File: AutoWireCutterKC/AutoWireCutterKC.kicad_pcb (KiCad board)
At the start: 2 copper layers, 17 parts, among them J1 LCD I/O, J2 ISP, J3 LCD Serial, J5 LCD Power, J6 Servo, J8 Barrel_Jack, J9 Stepper, U1 ATMEGA328P-AU, U2 MCP1700_SOT23, U3 LT1129-5.0_SOT223

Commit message: PCB Populated
Traces needed
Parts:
- removed J3: LCD Serial, Pin_Headers:Pin_Header_Angled_1x02_Pitch2.54mm
- removed J5: LCD Power, Pin_Headers:Pin_Header_Angled_1x02_Pitch2.54mm
- removed J6: Servo, Pin_Headers:Pin_Header_Angled_1x03_Pitch2.54mm
- added +5v: LCD Power, Pin_Headers:Pin_Header_Angled_1x02_Pitch2.54mm, F.Cu at (159.5, 117.3)
- added RX: LCD Serial, Pin_Headers:Pin_Header_Angled_1x02_Pitch2.54mm, F.Cu at (167.1, 117.3)
- added Servo: Servo, Pin_Headers:Pin_Header_Angled_1x03_Pitch2.54mm, F.Cu at (148.3, 117.3)
- moved C3 54.8 mm to (166.4, 81.3), turned to 180 degrees
- moved U3 51.5 mm to (170.2, 100.3), turned to 270 degrees
- moved C5 49.4 mm to (170.2, 94.0), turned to 180 degrees
- moved C1 41.5 mm to (161.3, 90.2)
- moved C2 39.4 mm to (158.8, 85.1)
- moved U2 29.3 mm to (166.4, 85.1), turned to 90 degrees
- moved C4 27.1 mm to (156.2, 90.2)
- moved C6 23.2 mm to (168.9, 90.2)
- moved J1 22.7 mm to (160.0, 105.4)
- moved J2 18.0 mm to (168.9, 108.0)
- moved A1 16.4 mm to (137.7, 96.0)
- moved U1 8.77 mm to (158.0, 97.0)
- moved J8 7.64 mm to (147.3, 91.4), turned to 180 degrees
- moved J9 5.61 mm to (154.9, 105.4)
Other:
- board outline added: 39.1 x 41.7 mm
- board text added: "Auto Wire Cutter"
- board text added: "BRW"

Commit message: Moving around footprints
Changing spacing and connectors
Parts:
- Servo: footprint Pin_Headers:Pin_Header_Angled_1x03_Pitch2.54mm -> Connectors_JST:JST_PH_S3B-PH-SM4-TB_03x2.00mm_Angled
- moved J2 18.3 mm to (165.6, 89.9)
- moved U3 17.5 mm to (166.1, 83.3)
- moved U2 16.2 mm to (150.4, 87.9)
- moved C3 12.3 mm to (156.0, 87.9)
- moved C6 11.2 mm to (160.5, 82.8), turned to 90 degrees
- moved C5 10.7 mm to (160.5, 89.4), turned to 270 degrees
- moved C1 10.5 mm to (150.9, 91.4)
- moved J1 7.73 mm to (165.6, 100.1)
- moved C2 6.02 mm to (153.4, 82.3)
- moved J8 4.06 mm to (143.3, 91.4)
- moved J9 0.57 mm to (155.4, 105.7)
- moved C4 0.36 mm to (156.0, 90.4)

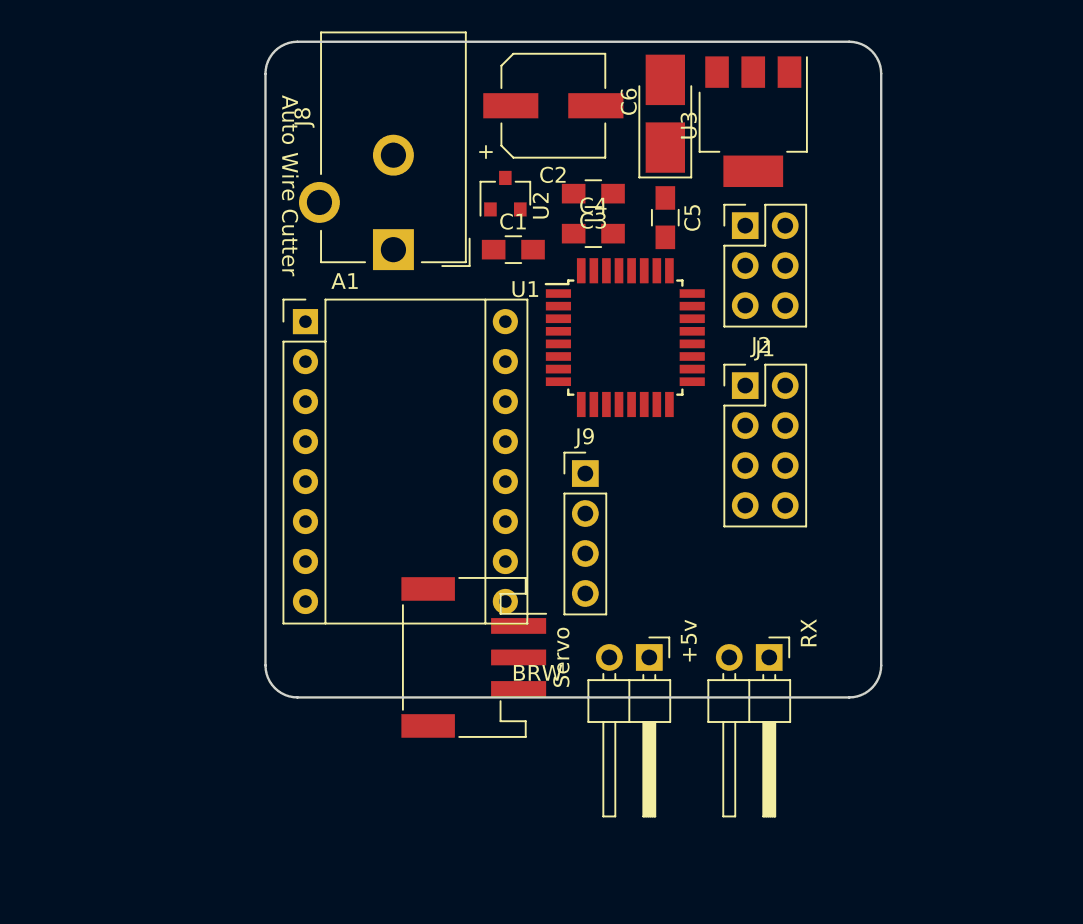
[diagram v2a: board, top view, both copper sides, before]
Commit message: PCB Redesign
Started on traces
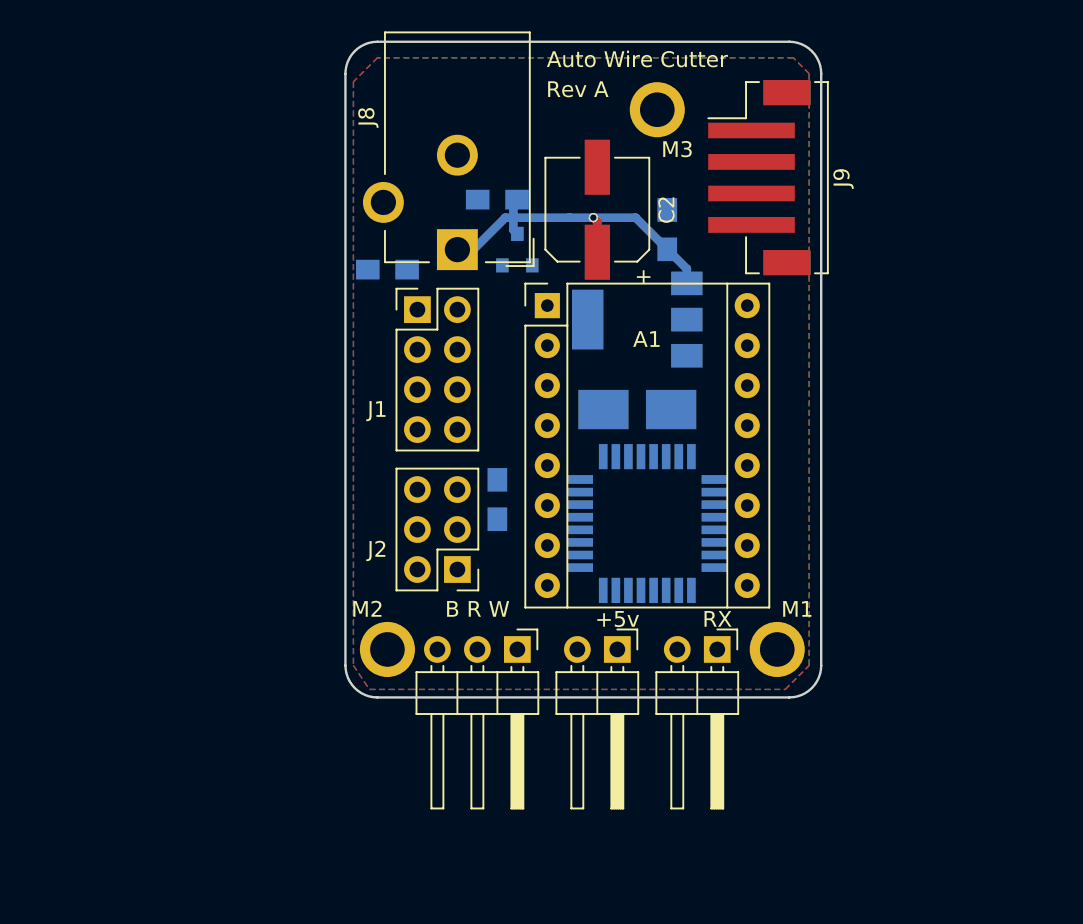
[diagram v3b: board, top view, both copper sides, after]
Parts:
- added M1: MountingHole_2.2mm_M2_ISO7380_Pad, Mounting_Holes:MountingHole_2.2mm_M2_ISO7380_Pad, F.Cu at (167.6, 116.8)
- added M2: MountingHole_2.2mm_M2_ISO7380_Pad, Mounting_Holes:MountingHole_2.2mm_M2_ISO7380_Pad, F.Cu at (142.9, 116.8)
- added M3: MountingHole_2.2mm_M2_ISO7380_Pad, Mounting_Holes:MountingHole_2.2mm_M2_ISO7380_Pad, F.Cu at (160.0, 82.5)
- B R W: renamed from Servo; footprint Connectors_JST:JST_PH_S3B-PH-SM4-TB_03x2.00mm_Angled -> Pin_Headers:Pin_Header_Angled_1x03_Pitch2.54mm
- C1, C3, C4, C5, C6, U1, U2, U3: moved to B.Cu
- J9: footprint Pin_Headers:Pin_Header_Straight_1x04_Pitch2.54mm -> Connectors_JST:JST_PH_B4B-PH-SM4-TB_04x2.00mm_Straight
- moved J2 28.5 mm to (147.3, 111.8), turned to 180 degrees
- moved J9 22.1 mm to (167.1, 86.9), turned to 270 degrees
- moved J1 21.4 mm to (144.8, 95.2)
- moved C6 18.9 mm to (158.8, 101.6), turned to 180 degrees
- moved C1 15.9 mm to (149.9, 107.3), turned to 90 degrees
- moved A1 15.4 mm to (153.0, 95.0)
- moved U3 14.6 mm to (158.8, 95.9), turned to 180 degrees
- moved C4 13.3 mm to (142.9, 92.7), turned to 180 degrees
- moved U1 11.9 mm to (159.4, 108.8), turned to 90 degrees
- moved C2 7.17 mm to (156.2, 88.9), turned to 90 degrees
- moved C3 6.11 mm to (149.9, 88.3)
- moved J8 4.06 mm to (147.3, 91.4)
- moved U2 3.64 mm to (151.1, 91.4)
- moved RX 3.34 mm to (163.8, 116.8)
- moved B R W 2.84 mm to (151.1, 116.8)
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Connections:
- J2 pad 2: +3V3 -> +5VL
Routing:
- net +12V: track 0.00 -> 22.4 mm, vias 0 -> 1
- added copper zone on F.Cu, net +5VL
- added copper zone on B.Cu, net GND
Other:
- board size 39.1 x 41.7 mm -> 30.2 x 41.7 mm
- net class 12v added: clearance 0.5, trace_width 0.55, via_dia 0.6, via_drill 0.4
- board text added: "Rev A"
- board text removed: "BRW"

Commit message: Rewiring - Layout changed again...
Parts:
- C1: moved to F.Cu
- J9: moved to B.Cu
- moved B R W 18.9 mm to (167.6, 107.7), turned to 0 degrees
- moved U1 16.6 mm to (142.7, 109.2), turned to 0 degrees
- moved C1 14.3 mm to (136.1, 111.3), turned to 270 degrees
- moved +5v 12.7 mm to (144.8, 116.8)
- moved RX 11.9 mm to (151.9, 116.8)
- moved C2 11.8 mm to (167.1, 84.3), turned to 270 degrees
- moved A1 11.8 mm to (162.1, 102.6), turned to 180 degrees
- moved M3 11.2 mm to (148.8, 81.3)
- moved J2 10.2 mm to (157.5, 110.7), turned to 0 degrees
- moved J9 9.16 mm to (167.6, 96.0), turned to 90 degrees
- moved J1 8.53 mm to (139.7, 102.1), turned to 180 degrees
- moved C5 7.10 mm to (155.4, 95.0), turned to 180 degrees
- moved U2 6.19 mm to (145.3, 93.5)
- moved U3 5.66 mm to (154.9, 100.1)
- moved J8 5.59 mm to (141.7, 91.4)
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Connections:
- J9 pad 1: Net-(A1-Pad4) -> Net-(A1-Pad3)
- J9 pad 2: Net-(A1-Pad3) -> Net-(A1-Pad4)
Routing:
- net Net-(J1-Pad4): track 0.00 -> 37.0 mm, vias 0 -> 2
- net Net-(A1-Pad9): track 0.00 -> 35.2 mm, vias 0 -> 1
- net Net-(J6-Pad1): track 0.00 -> 33.5 mm, vias 0 -> 1
- net Net-(J1-Pad6): track 0.00 -> 33.5 mm
- net Net-(J1-Pad5): track 0.00 -> 26.9 mm, vias 0 -> 1
- net +12V: track 22.4 -> 0.00 mm, vias 1 -> 0
- net Net-(J1-Pad7): track 0.00 -> 20.9 mm, vias 0 -> 1
- net Net-(J2-Pad5): track 0.00 -> 18.3 mm, vias 0 -> 1
- net Net-(J1-Pad8): track 0.00 -> 13.8 mm
- net Net-(J3-Pad1): track 0.00 -> 12.4 mm
- net Net-(J3-Pad2): track 0.00 -> 11.1 mm
- net Net-(J1-Pad2): track 0.00 -> 9.52 mm
- net Net-(J1-Pad3): track 0.00 -> 8.05 mm
- net Net-(J1-Pad1): track 0.00 -> 4.41 mm
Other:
- board size 30.2 x 41.7 mm -> 35.8 x 41.7 mm
- net class 12v: trace_width 0.55 -> 0.75; via_dia 0.6 -> 1; via_drill 0.4 -> 0.8
- net class MotorLeads added: clearance 0.25, trace_width 0.4, via_dia 0.6, via_drill 0.4

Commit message: Update bad file
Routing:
- net Net-(A1-Pad15): track 0.00 -> 25.2 mm, vias 0 -> 2
- net Net-(A1-Pad16): track 0.00 -> 20.6 mm, vias 0 -> 2
- net GND: track 0.00 -> 5.22 mm, vias 0 -> 2
- net +5VL: track 0.00 -> 3.83 mm, vias 0 -> 2
- net Net-(A1-Pad9): track 35.2 -> 38.9 mm, vias 1 -> 3
- net Net-(J1-Pad6): track 33.5 -> 33.3 mm, vias 0 -> 1

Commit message: Schematic almost done
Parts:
- M1, M2, M3: value MountingHole_2.2mm_M2_ISO7380_Pad -> Conn_01x01_Male
- moved M3 3.14 mm to (151.9, 80.5)
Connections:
- M1 pad 1: (no net) -> GND
- M2 pad 1: (no net) -> GND
- M3 pad 1: (no net) -> GND
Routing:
- net +12V: track 0.00 -> 58.1 mm, vias 0 -> 1
- net +5V: track 0.00 -> 14.2 mm
- net GND: track 5.22 -> 15.3 mm, vias 2 -> 3
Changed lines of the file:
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@@
 (kicad_pcb (version 4) (host pcbnew 4.0.7)
   (general
-    (links 59)
-    (no_connects 21)
-    (area 122.501333 76.714999 182.298667 127.915001)
+    (links 62)
+    (no_connects 10)
+    (area 134.544999 78.156999 170.509001 119.963001)
     (thickness 1.6)
     (drawings 12)
-    (tracks 131)
+    (tracks 164)
     (zones 0)
     (modules 20)
@@
   (page A4)
   (layers
-    (0 F.Cu signal hide)
+    (0 F.Cu signal)
     (31 B.Cu signal)
     (32 B.Adhes user)
@@
   )
   (module Mounting_Holes:MountingHole_2.2mm_M2_ISO7380_Pad (layer F.Cu)
-    (at 148.844 81.28)
+    (at 151.892 80.518)
     (descr "Mounting Hole 2.2mm, M2, ISO7380")
     (tags "mounting hole 2.2mm m2 iso7380")
     (attr virtual)
-    (fp_text reference M3 (at 1.27 2.54) (layer F.SilkS)
-      (effects (font (size 1 1) (thickness 0.15)))
-    )
-    (fp_text value MountingHole_2.2mm_M2_ISO7380_Pad (at 0 2.75) (layer F.Fab)
+    (fp_text reference M3 (at -3.302 -0.762) (layer F.SilkS)
+      (effects (font (size 1 1) (thickness 0.15)))
+    )
+    (fp_text value Conn_01x01_Male (at 0 2.75) (layer F.Fab)
       (effects (font (size 1 1) (thickness 0.15)))
     )
@@
     (fp_circle (center 0 0) (end 1.75 0) (layer Cmts.User) (width 0.15))
     (fp_circle (center 0 0) (end 2 0) (layer F.CrtYd) (width 0.05))
-    (pad 1 thru_hole circle (at 0 0) (size 3.5 3.5) (drill 2.2) (layers *.Cu *.Mask))
+    (pad 1 thru_hole circle (at 0 0) (size 3.5 3.5) (drill 2.2) (layers *.Cu *.Mask)
+      (net 1 GND))
+  )
+  (module Mounting_Holes:MountingHole_2.2mm_M2_ISO7380_Pad (layer F.Cu)
+    (at 167.132 116.84)
+    (descr "Mounting Hole 2.2mm, M2, ISO7380")
+    (tags "mounting hole 2.2mm m2 iso7380")
+    (attr virtual)
+    (fp_text reference M1 (at 1.27 -2.54) (layer F.SilkS)
+      (effects (font (size 1 1) (thickness 0.15)))
+    )
+    (fp_text value Conn_01x01_Male (at 0 2.75) (layer F.Fab)
+      (effects (font (size 1 1) (thickness 0.15)))
+    )
+    (fp_text user %R (at 0.3 0) (layer F.Fab)
+      (effects (font (size 1 1) (thickness 0.15)))
+    )
+    (fp_circle (center 0 0) (end 1.75 0) (layer Cmts.User) (width 0.15))
+    (fp_circle (center 0 0) (end 2 0) (layer F.CrtYd) (width 0.05))
+    (pad 1 thru_hole circle (at 0 0) (size 3.5 3.5) (drill 2.2) (layers *.Cu *.Mask)
+      (net 1 GND))
   )
   (module Mounting_Holes:MountingHole_2.2mm_M2_ISO7380_Pad (layer F.Cu)
@@
       (effects (font (size 1 1) (thickness 0.15)))
     )
-    (fp_text value MountingHole_2.2mm_M2_ISO7380_Pad (at 0 2.75) (layer F.Fab)
+    (fp_text value Conn_01x01_Male (at 0 2.75) (layer F.Fab)
       (effects (font (size 1 1) (thickness 0.15)))
     )
@@
     (fp_circle (center 0 0) (end 2 0) (layer F.CrtYd) (width 0.05))
     (pad 1 thru_hole circle (at 0 0) (size 3.5 3.5) (drill 2.2) (layers *.Cu *.Mask)
-      (zone_connect 2))
+      (net 1 GND) (zone_connect 2))
   )
   (module Modules:Pololu_Breakout-16_15.2x20.3mm (layer F.Cu)
@@
     )
   )
-  (module Mounting_Holes:MountingHole_2.2mm_M2_ISO7380_Pad (layer F.Cu)
-    (at 167.132 116.84)
-    (descr "Mounting Hole 2.2mm, M2, ISO7380")
-    (tags "mounting hole 2.2mm m2 iso7380")
-    (attr virtual)
-    (fp_text reference M1 (at 1.27 -2.54) (layer F.SilkS)
-      (effects (font (size 1 1) (thickness 0.15)))
-    )
-    (fp_text value MountingHole_2.2mm_M2_ISO7380_Pad (at 0 2.75) (layer F.Fab)
-      (effects (font (size 1 1) (thickness 0.15)))
-    )
-    (fp_text user %R (at 0.3 0) (layer F.Fab)
-      (effects (font (size 1 1) (thickness 0.15)))
-    )
-    (fp_circle (center 0 0) (end 1.75 0) (layer Cmts.User) (width 0.15))
-    (fp_circle (center 0 0) (end 2 0) (layer F.CrtYd) (width 0.05))
-    (pad 1 thru_hole circle (at 0 0) (size 3.5 3.5) (drill 2.2) (layers *.Cu *.Mask))
-  )
   (gr_arc (start 136.652 117.856) (end 136.652 119.888) (angle 90) (layer Edge.Cuts) (width 0.15))
   (gr_arc (start 136.652 80.264) (end 134.62 80.264) (angle 90) (layer Edge.Cuts) (width 0.15))
@@
   (gr_line (start 142.24 78.232) (end 136.652 78.232) (angle 90) (layer Edge.Cuts) (width 0.15))
   (gr_line (start 142.24 119.888) (end 136.652 119.888) (angle 90) (layer Edge.Cuts) (width 0.15))
-  (gr_text "Rev A" (at 155.448 81.28) (layer F.SilkS)
+  (gr_text "Rev A" (at 156.21 81.28) (layer F.SilkS)
     (effects (font (size 1 1) (thickness 0.15)))
   )
   (gr_line (start 168.402 78.232) (end 142.24 78.232) (angle 90) (layer Edge.Cuts) (width 0.15))
   (gr_line (start 168.402 119.888) (end 142.24 119.888) (angle 90) (layer Edge.Cuts) (width 0.15))
-  (gr_text "Auto Wire Cutter" (at 158.75 79.375) (layer F.SilkS)
+  (gr_text "Auto Wire Cutter" (at 160.02 79.502) (layer F.SilkS)
     (effects (font (size 1 1) (thickness 0.15)))
   )
@@
   (gr_arc (start 168.402 117.856) (end 170.434 117.856) (angle 90) (layer Edge.Cuts) (width 0.15))
   (gr_line (start 170.434 117.856) (end 170.434 80.264) (angle 90) (layer Edge.Cuts) (width 0.15))
+  (segment (start 146.998 109.62) (end 148.482 109.62) (width 0.25) (layer B.Cu) (net 1) (status 400000))
+  (via (at 148.59 113.792) (size 0.6) (drill 0.4) (layers F.Cu B.Cu) (net 1))
+  (segment (start 148.59 109.728) (end 148.59 113.792) (width 0.25) (layer B.Cu) (net 1))
+  (segment (start 148.482 109.62) (end 148.59 109.728) (width 0.25) (layer B.Cu) (net 1))
+  (segment (start 138.498 110.42) (end 139.884 110.42) (width 0.25) (layer B.Cu) (net 1) (status 400000))
+  (segment (start 139.808 108.82) (end 138.498 108.82) (width 0.25) (layer B.Cu) (net 1) (status 800000))
+  (segment (start 139.954 108.966) (end 139.808 108.82) (width 0.25) (layer B.Cu) (net 1))
+  (segment (start 139.954 110.35) (end 139.954 108.966) (width 0.25) (layer B.Cu) (net 1))
+  (segment (start 139.884 110.42) (end 139.954 110.35) (width 0.25) (layer B.Cu) (net 1))
   (via (at 137.922 114.046) (size 0.6) (drill 0.4) (layers F.Cu B.Cu) (net 1))
   (segment (start 137.922 114.046) (end 136.378 112.502) (width 0.25) (layer F.Cu) (net 1))
@@
   (segment (start 137.192 111.22) (end 135.89 109.918) (width 0.25) (layer B.Cu) (net 9))
   (segment (start 138.498 111.22) (end 137.192 111.22) (width 0.25) (layer B.Cu) (net 9))
+  (segment (start 141.732 91.44) (end 143.53 91.44) (width 0.75) (layer B.Cu) (net 10))
+  (segment (start 143.53 91.44) (end 144.546 90.424) (width 0.75) (layer B.Cu) (net 10))
+  (segment (start 144.546 90.424) (end 144.546 91.73) (width 0.75) (layer B.Cu) (net 10))
+  (segment (start 144.546 91.73) (end 145.288 92.472) (width 0.75) (layer B.Cu) (net 10))
+  (segment (start 156.718 85.09) (end 161.798 85.09) (width 0.75) (layer B.Cu) (net 10))
+  (segment (start 161.798 85.09) (end 162.052 84.836) (width 0.75) (layer B.Cu) (net 10))
+  (segment (start 156.718 85.09) (end 156.718 94.976) (width 0.75) (layer B.Cu) (net 10))
+  (segment (start 156.718 94.976) (end 158.09 96.348) (width 0.75) (layer B.Cu) (net 10))
+  (segment (start 158.09 96.348) (end 158.09 97.776) (width 0.75) (layer B.Cu) (net 10))
+  (segment (start 141.732 91.44) (end 141.732 89.154) (width 0.75) (layer B.Cu) (net 10))
+  (segment (start 160.18 81.628) (end 167.132 81.628) (width 0.75) (layer F.Cu) (net 10))
+  (segment (start 156.718 85.09) (end 160.18 81.628) (width 0.75) (layer F.Cu) (net 10))
+  (via (at 156.718 85.09) (size 1) (drill 0.8) (layers F.Cu B.Cu) (net 10))
+  (segment (start 152.4 85.09) (end 156.718 85.09) (width 0.75) (layer B.Cu) (net 10))
+  (segment (start 149.86 82.55) (end 152.4 85.09) (width 0.75) (layer B.Cu) (net 10))
+  (segment (start 146.812 82.55) (end 149.86 82.55) (width 0.75) (layer B.Cu) (net 10))
+  (segment (start 144.526 84.836) (end 146.812 82.55) (width 0.75) (layer B.Cu) (net 10))
+  (segment (start 144.526 86.36) (end 144.526 84.836) (width 0.75) (layer B.Cu) (net 10))
+  (segment (start 141.732 89.154) (end 144.526 86.36) (width 0.75) (layer B.Cu) (net 10))
   (segment (start 138.498 112.02) (end 140.964 112.02) (width 0.25) (layer B.Cu) (net 11))
   (segment (start 149.352 103.886) (end 149.352 102.616) (width 0.25) (layer B.Cu) (net 11))
@@
   (segment (start 142.748 110.236) (end 144.526 110.236) (width 0.25) (layer B.Cu) (net 11))
   (segment (start 140.964 112.02) (end 142.748 110.236) (width 0.25) (layer B.Cu) (net 11))
+  (segment (start 158.09 102.376) (end 158.09 104.36) (width 0.25) (layer B.Cu) (net 12))
+  (segment (start 158.09 104.36) (end 159.394 105.664) (width 0.25) (layer B.Cu) (net 12))
+  (segment (start 159.394 105.664) (end 159.394 106.054) (width 0.25) (layer B.Cu) (net 12))
+  (segment (start 159.394 106.054) (end 163.576 110.236) (width 0.25) (layer B.Cu) (net 12))
+  (segment (start 163.576 110.236) (end 167.64 110.236) (width 0.25) (layer B.Cu) (net 12))
   (segment (start 142.348 104.97) (end 142.348 103.994) (width 0.25) (layer B.Cu) (net 13))
   (segment (start 142.348 103.994) (end 140.462 102.108) (width 0.25) (layer B.Cu) (net 13))
